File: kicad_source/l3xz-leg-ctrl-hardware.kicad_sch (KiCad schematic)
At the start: 38 parts, among them CN1 ARDUINO_NANO_33, CN2 SM04B-SRSS-TB, CN3 SM04B-SRSS-TB, CN6 691322310002, CN7 CONN_02X03, CN8 WAGO 733-362, U3 24LC64

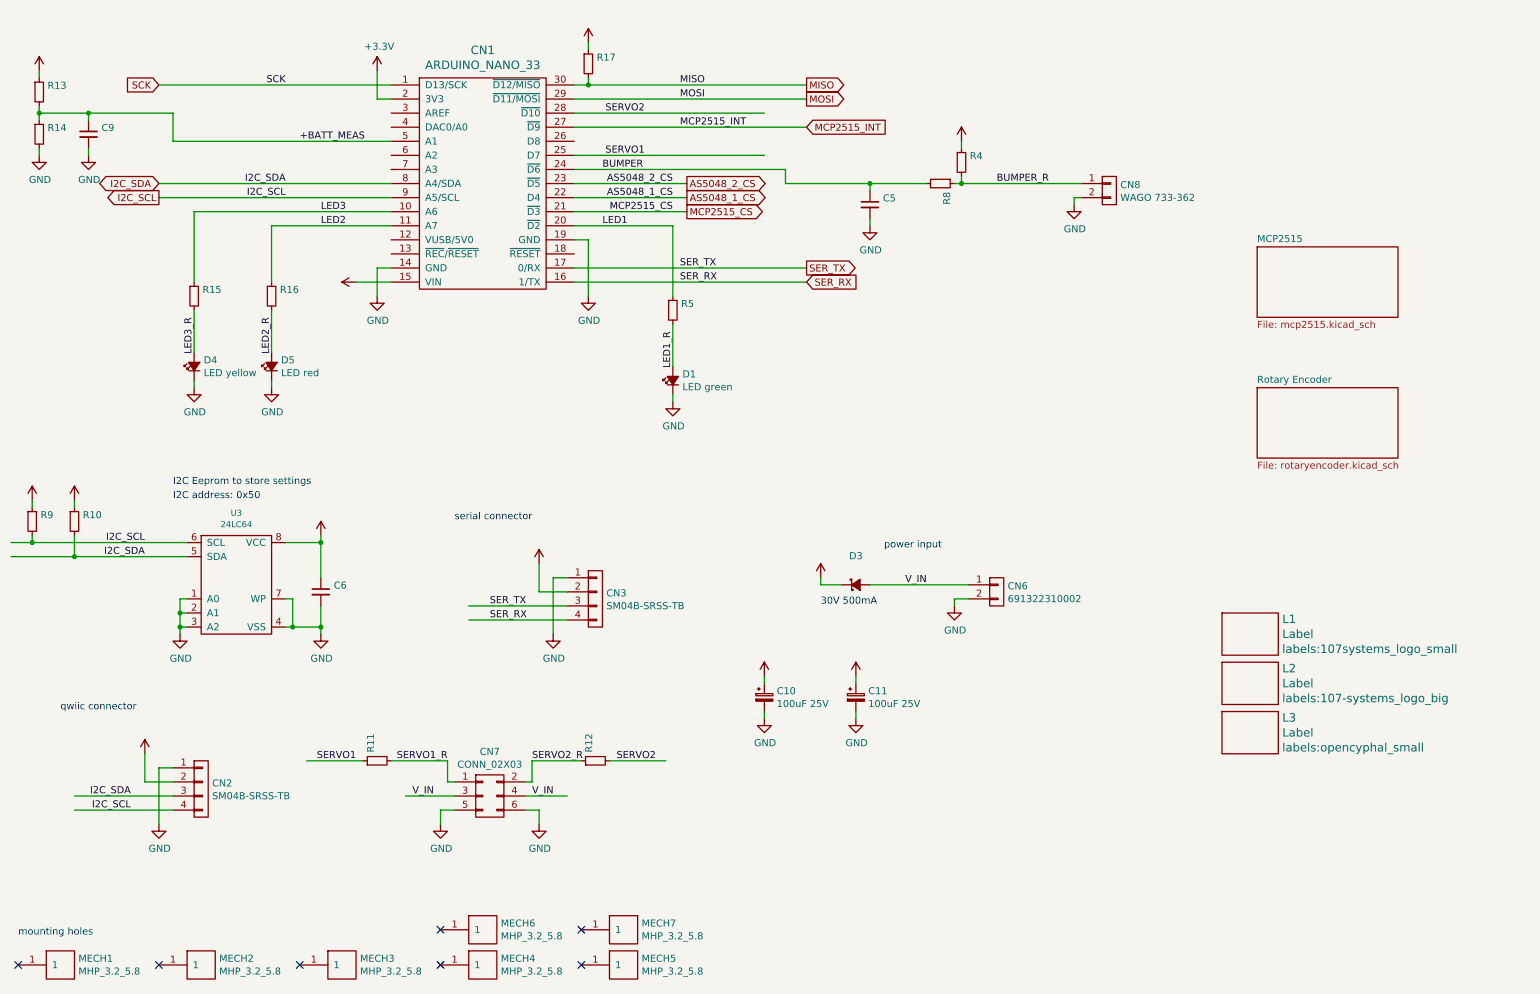
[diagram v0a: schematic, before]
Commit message: updated some symbol library links
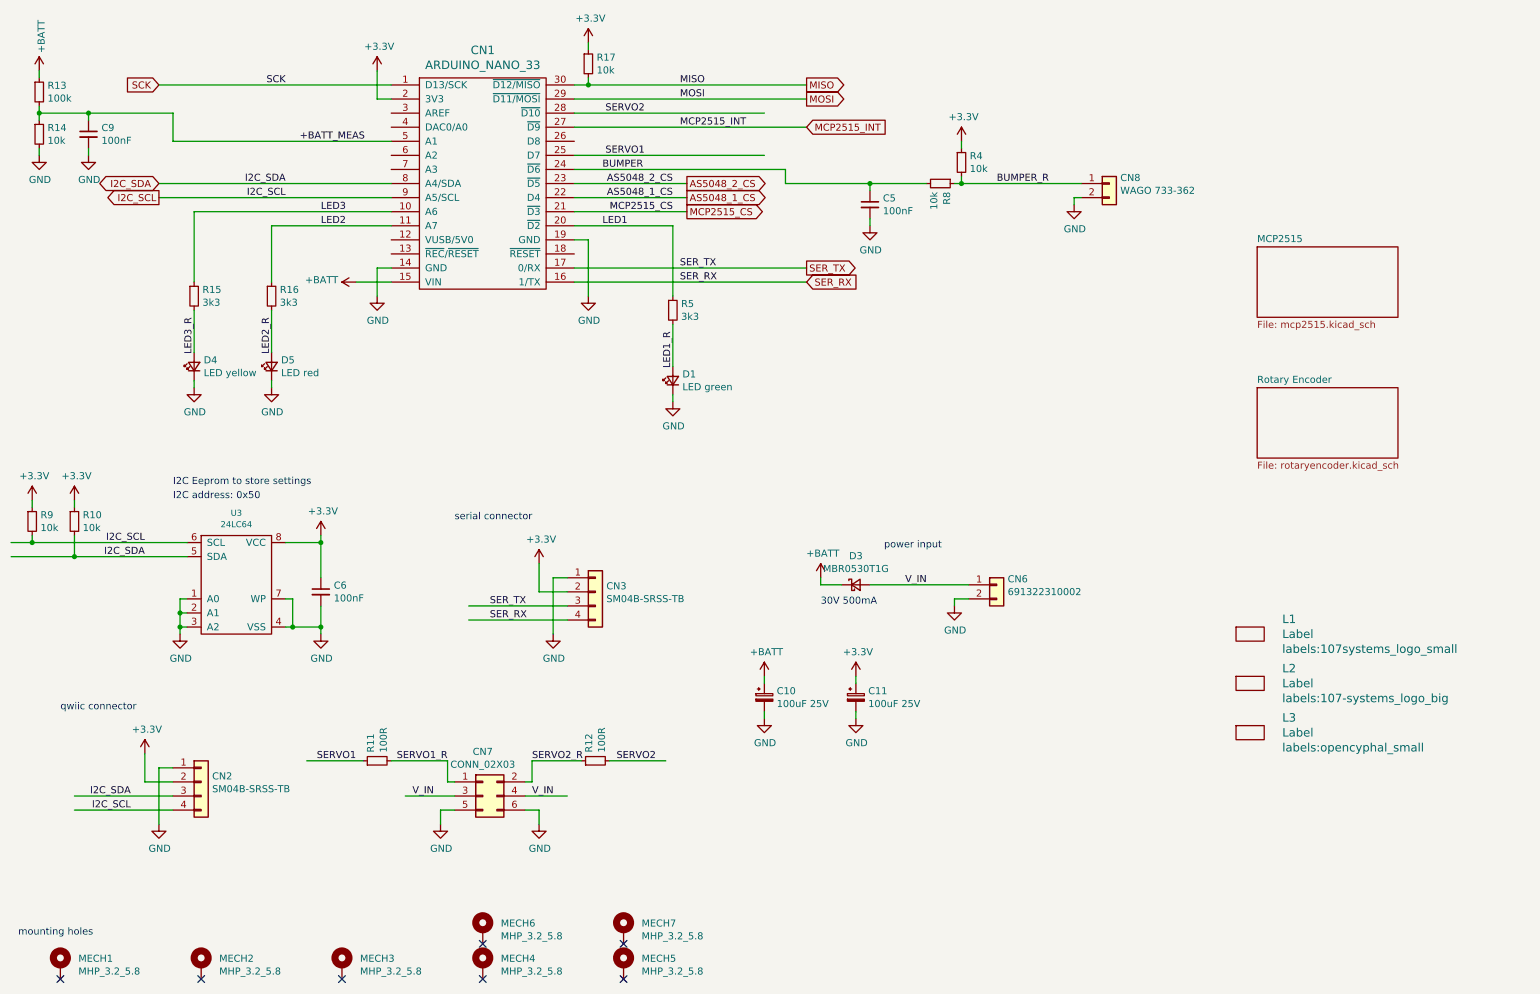
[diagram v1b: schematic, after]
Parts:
- C10, C11: symbol l3xz-leg-ctrl-hardware-rescue:CP_Small-devices -> Device:C_Polarized_Small
- C5, C6, C9: value (none) -> 100nF; footprint (none) -> capacitors:C_0603; symbol l3xz-leg-ctrl-hardware-rescue:C_0603-devices -> Device:C_Small
- CN2, CN3: symbol l3xz-leg-ctrl-hardware-rescue:CONN_01X04-mechanical-connectors -> Connector_Generic:Conn_01x04
- CN6, CN8: symbol l3xz-leg-ctrl-hardware-rescue:CONN_01X02-mechanical-connectors -> Connector_Generic:Conn_01x02
- CN7: symbol l3xz-leg-ctrl-hardware-rescue:CONN_02X03-mechanical-connectors -> Connector_Generic:Conn_02x03_Odd_Even
- D1, D4, D5: symbol l3xz-leg-ctrl-hardware-rescue:Led_Small-devices -> Device:LED_Small
- D3: value (none) -> MBR0530T1G; footprint (none) -> diodes:SOD-123; symbol l3xz-leg-ctrl-hardware-rescue:D_Schottky_Small-devices -> Device:D_Schottky_Small
- L1, L2, L3: symbol l3xz-leg-ctrl-hardware-rescue:Label-devices -> generationmake:Label
- MECH1, MECH2, MECH3, MECH4, MECH5, MECH6, MECH7: symbol l3xz-leg-ctrl-hardware-rescue:MHP_3.2_5.8-MECH_mounting-holes -> Mechanical:MountingHole_Pad
- R10, R14, R17, R4, R8, R9: value (none) -> 10k; footprint (none) -> resistors:R_0603; symbol l3xz-leg-ctrl-hardware-rescue:R_0603-devices -> Device:R_Small
- R11, R12: value (none) -> 100R; footprint (none) -> resistors:R_0603; symbol l3xz-leg-ctrl-hardware-rescue:R_0603-devices -> Device:R_Small
- R13: value (none) -> 100k; footprint (none) -> resistors:R_0603; symbol l3xz-leg-ctrl-hardware-rescue:R_0603-devices -> Device:R_Small
- R15, R16, R5: value (none) -> 3k3; footprint (none) -> resistors:R_0603; symbol l3xz-leg-ctrl-hardware-rescue:R_0603-devices -> Device:R_Small
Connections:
- net +3V3 renamed +3.3V

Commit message: updated footprint library
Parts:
- C10, C11: footprint capacitors:c_elec_8x10 -> Capacitor_SMD:CP_Elec_8x10
- C5, C6, C9: footprint capacitors:C_0603 -> Capacitor_SMD:C_0603_1608Metric
- CN2, CN3: footprint connectors_JST_SH:Connectors_JST_SM04B-SRSS-TB -> Connector_JST:JST_SH_SM04B-SRSS-TB_1x04-1MP_P1.00mm_Horizontal
- CN7: footprint pin_headers:Pin_Header_Angled_2x03 -> Connector_PinHeader_2.54mm:PinHeader_2x03_P2.54mm_Horizontal
- D3: footprint diodes:SOD-123 -> Diode_SMD:D_SOD-123
- R10, R11, R12, R13, R14, R15, R16, R17, R4, R5, R8, R9: footprint resistors:R_0603 -> Resistor_SMD:R_0603_1608Metric
- U3: footprint SOIC:SOIC-8_3.9x4.9mm_Pitch1.27mm -> Package_SO:SOIC-8_3.9x4.9mm_P1.27mm

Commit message: connected mounting pads of connectors
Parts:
- CN2, CN3: symbol Connector_Generic:Conn_01x04 -> Connector_Generic_MountingPin:Conn_01x04_MountingPin
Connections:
- new net MP1: CN2.MP (MountPin), CN3.MP (MountPin)
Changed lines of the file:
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@@
+    (stroke (width 0) (type default) (color 0 0 0 0))
+  )
+  (wire (pts (xy 50.8 170.18) (xy 57.15 170.18))
     (stroke (width 0) (type default) (color 0 0 0 0))
   )
@@
     (stroke (width 0) (type default) (color 0 0 0 0))
   )
+  (wire (pts (xy 121.92 135.89) (xy 128.27 135.89))
+    (stroke (width 0) (type default) (color 0 0 0 0))
+  )
   (wire (pts (xy 99.06 128.27) (xy 116.84 128.27))
     (stroke (width 0) (type default) (color 0 0 0 0))
@@
     (effects (font (size 1.27 1.27)) (justify left bottom))
   )
+  (label "MP1" (at 123.19 135.89 0)
+    (effects (font (size 1.27 1.27)) (justify left bottom))
+  )
   (label "SERVO2_R" (at 110.49 156.21 0)
     (effects (font (size 1.27 1.27)) (justify left bottom))
@@
   (label "AS5048_2_CS" (at 135.89 52.07 180)
     (effects (font (size 1.27 1.27)) (justify right bottom))
+  )
+  (label "MP1" (at 52.07 170.18 0)
+    (effects (font (size 1.27 1.27)) (justify left bottom))
   )
   (label "+BATT_MEAS" (at 68.58 44.45 0)
@@
     (pin "1")
   )
-  (symbol (lib_id "Connector_Generic:Conn_01x04") (at 121.92 125.73 0) (unit 1)
+  (symbol (lib_id "Connector_Generic_MountingPin:Conn_01x04_MountingPin") (at 121.92 125.73 0) (unit 1)
     (in_bom yes) (on_board yes)
     (property "Reference" "CN3" (id 0) (at 123.9012 124.6886 0)
@@
       (effects (font (size 1.27 1.27)) hide)
     )
-    (property "Datasheet" "" (id 3) (at 121.92 125.73 0))
+    (property "Datasheet" "~" (id 3) (at 121.92 125.73 0)
+      (effects (font (size 1.27 1.27)) hide)
+    )
     (pin "1")
     (pin "2")
     (pin "3")
     (pin "4")
+    (pin "MP")
   )
   (symbol (lib_id "power:GND") (at 114.3 133.35 0) (unit 1)
@@
     (pin "1")
   )
-  (symbol (lib_id "Connector_Generic:Conn_01x04") (at 50.8 160.02 0) (unit 1)
+  (symbol (lib_id "Connector_Generic_MountingPin:Conn_01x04_MountingPin") (at 50.8 160.02 0) (unit 1)
     (in_bom yes) (on_board yes)
     (property "Reference" "CN2" (id 0) (at 52.7812 158.9786 0)
@@
       (effects (font (size 1.27 1.27)) hide)
     )
-    (property "Datasheet" "" (id 3) (at 50.8 160.02 0))
+    (property "Datasheet" "~" (id 3) (at 50.8 160.02 0)
+      (effects (font (size 1.27 1.27)) hide)
+    )
     (pin "1")
     (pin "2")
     (pin "3")
     (pin "4")
+    (pin "MP")
   )
   (symbol (lib_id "power:+3.3V") (at 40.64 154.94 0) (unit 1)

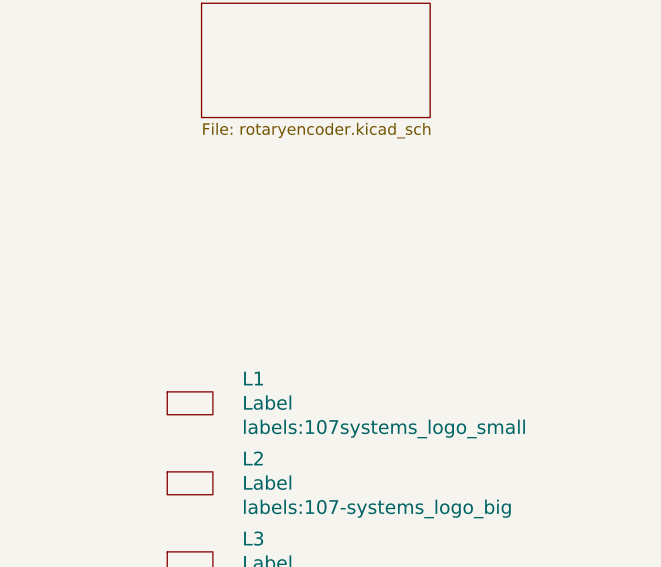
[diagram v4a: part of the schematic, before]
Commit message: added labels, updated pdf schematic and images
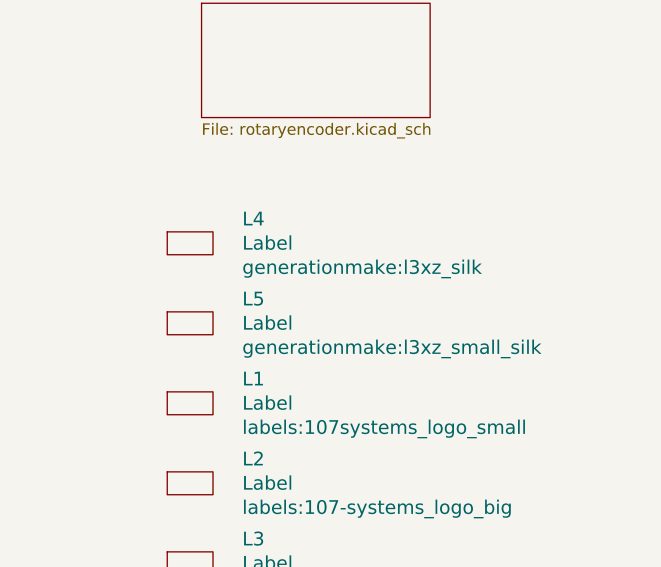
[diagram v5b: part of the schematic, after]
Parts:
- added L4: Label, generationmake:l3xz_silk, symbol generationmake:Label
- added L5: Label, generationmake:l3xz_small_silk, symbol generationmake:Label
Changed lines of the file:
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@@
   (title_block
     (title "l3xz-hw_leg-controller")
-    (date "2023-01-29")
-    (rev "dev_0.2")
+    (date "2023-01-30")
+    (rev "0.2")
     (company "107-systems")
   )
@@
     (pin "2")
   )
+  (symbol (lib_id "generationmake:Label") (at 240.03 115.57 0) (unit 1)
+    (in_bom yes) (on_board yes)
+    (property "Reference" "L4" (id 0) (at 245.8212 112.8776 0)
+      (effects (font (size 1.524 1.524)) (justify left))
+    )
+    (property "Value" "Label" (id 1) (at 245.8212 115.57 0)
+      (effects (font (size 1.524 1.524)) (justify left))
+    )
+    (property "Footprint" "generationmake:l3xz_silk" (id 2) (at 245.8212 118.2624 0)
+      (effects (font (size 1.524 1.524)) (justify left))
+    )
+    (property "Datasheet" "" (id 3) (at 240.03 115.57 0)
+      (effects (font (size 1.524 1.524)))
+    )
+  )
+  (symbol (lib_id "generationmake:Label") (at 240.03 124.46 0) (unit 1)
+    (in_bom yes) (on_board yes)
+    (property "Reference" "L5" (id 0) (at 245.8212 121.7676 0)
+      (effects (font (size 1.524 1.524)) (justify left))
+    )
+    (property "Value" "Label" (id 1) (at 245.8212 124.46 0)
+      (effects (font (size 1.524 1.524)) (justify left))
+    )
+    (property "Footprint" "generationmake:l3xz_small_silk" (id 2) (at 245.8212 127.1524 0)
+      (effects (font (size 1.524 1.524)) (justify left))
+    )
+    (property "Datasheet" "" (id 3) (at 240.03 124.46 0)
+      (effects (font (size 1.524 1.524)))
+    )
+  )
   (sheet (at 241.3 63.5) (size 25.4 12.7) (fields_autoplaced)
     (stroke (width 0) (type solid) (color 0 0 0 0))
@@
       (reference "L3") (unit 1) (value "Label") (footprint "labels:opencyphal_small")
     )
+    (path "/30f2ab3d-3eed-4de9-b2fb-d092f4eb160a"
+      (reference "L4") (unit 1) (value "Label") (footprint "generationmake:l3xz_silk")
+    )
+    (path "/32418b59-9da7-4cd8-97f6-00b5eadf13ed"
+      (reference "L5") (unit 1) (value "Label") (footprint "generationmake:l3xz_small_silk")
+    )
     (path "/00000000-0000-0000-0000-00005e401602"
